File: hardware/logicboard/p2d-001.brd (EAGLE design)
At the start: 100 x 75 mm, 68 parts, among them IC1 74LS06N, IC2 4066N, IC3 MAX3468CPA, J1 MKR, J10 THS, J2 GPIO, J3 Vcc, J4 RLY, J5 SPI, J6 LED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

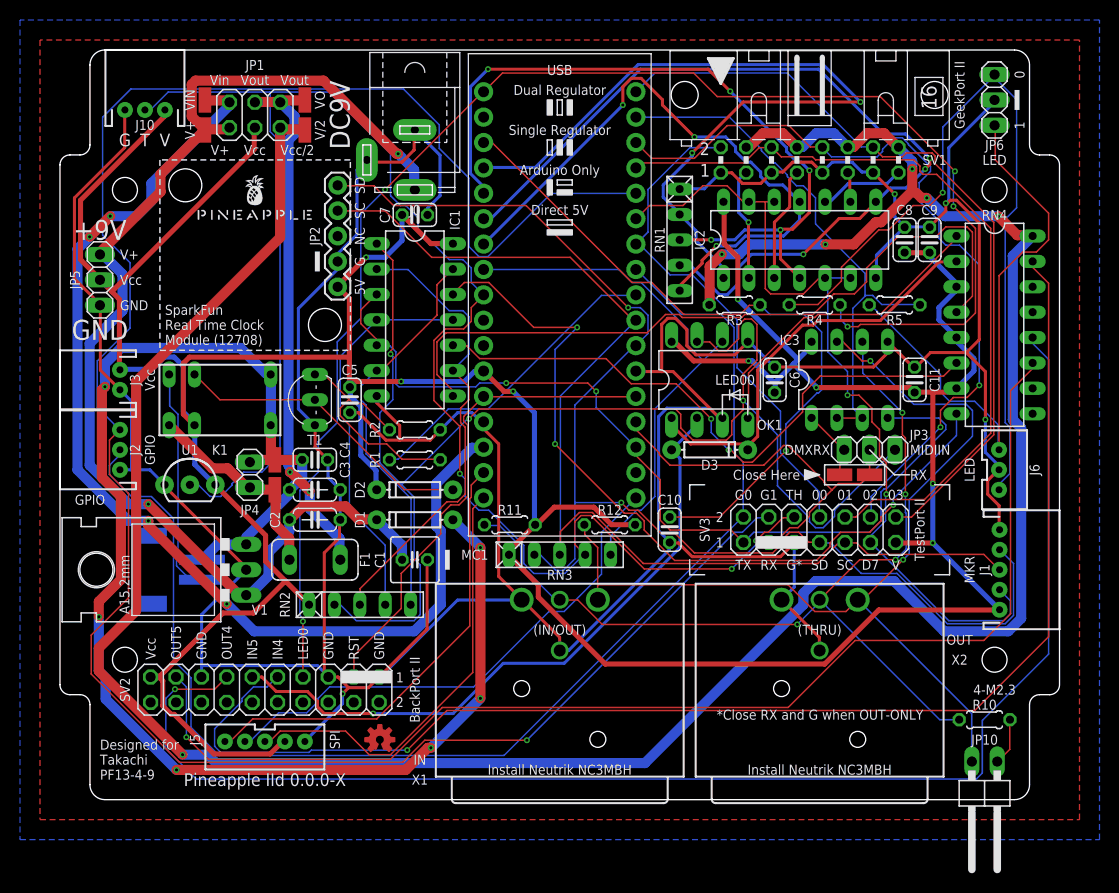
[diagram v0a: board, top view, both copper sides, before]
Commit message: Now DMX's Data- has pull-down R., not pull-up.
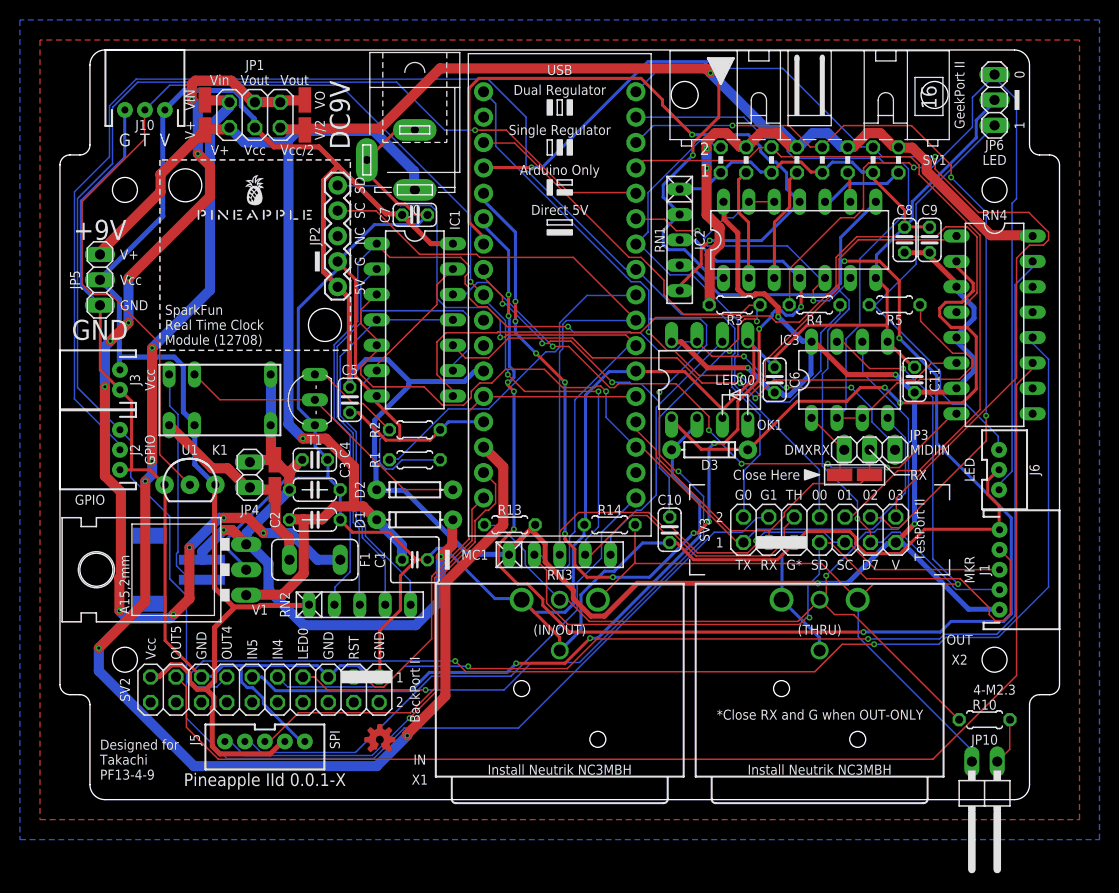
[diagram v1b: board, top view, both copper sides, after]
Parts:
- R13, R14: value 470 -> 22k
- renumbered R11 to R13, R12 to R14
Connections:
- net DATA-: now also R14.2; no longer R14.1
- net GND: now also R14.1
- net VCC: no longer R14.2
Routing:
- net VCC/2: track 275.6 -> 116.1 mm, vias 6 -> 3
- net VOUTRAW: track 146.2 -> 64.9 mm, vias 6 -> 2
- net ANLG2: track 87.7 -> 164.3 mm, vias 3 -> 8
- net VOUT: track 54.0 -> 102.2 mm, vias 2 -> 11
- net VCC: track 395.8 -> 361.9 mm, vias 8 -> 5
- net MIN: track 136.2 -> 103.7 mm, vias 3 -> 4
- net LED1: track 54.9 -> 82.3 mm
- net ANLG1: track 74.2 -> 101.3 mm, vias 5 -> 11
- net VIN: track 110.1 -> 134.6 mm, vias 4 -> 5
- net MISND: track 137.1 -> 113.5 mm, vias 1 -> 2
- net ANLG0: track 78.7 -> 57.2 mm, vias 2 -> 3
- net MOSND: track 142.2 -> 120.9 mm, vias 1 -> 2
- net N$4: track 81.1 -> 62.0 mm, vias 3 -> 5
- net GPIO1: track 213.0 -> 195.1 mm
- net SDA: track 127.5 -> 143.0 mm
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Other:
- board text added: "Pineapple IId 0.0.1-X"
- board text removed: "Pineapple IId 0.0.0-X"

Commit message: Changed DMX pull-up/down resisters to surface mount.
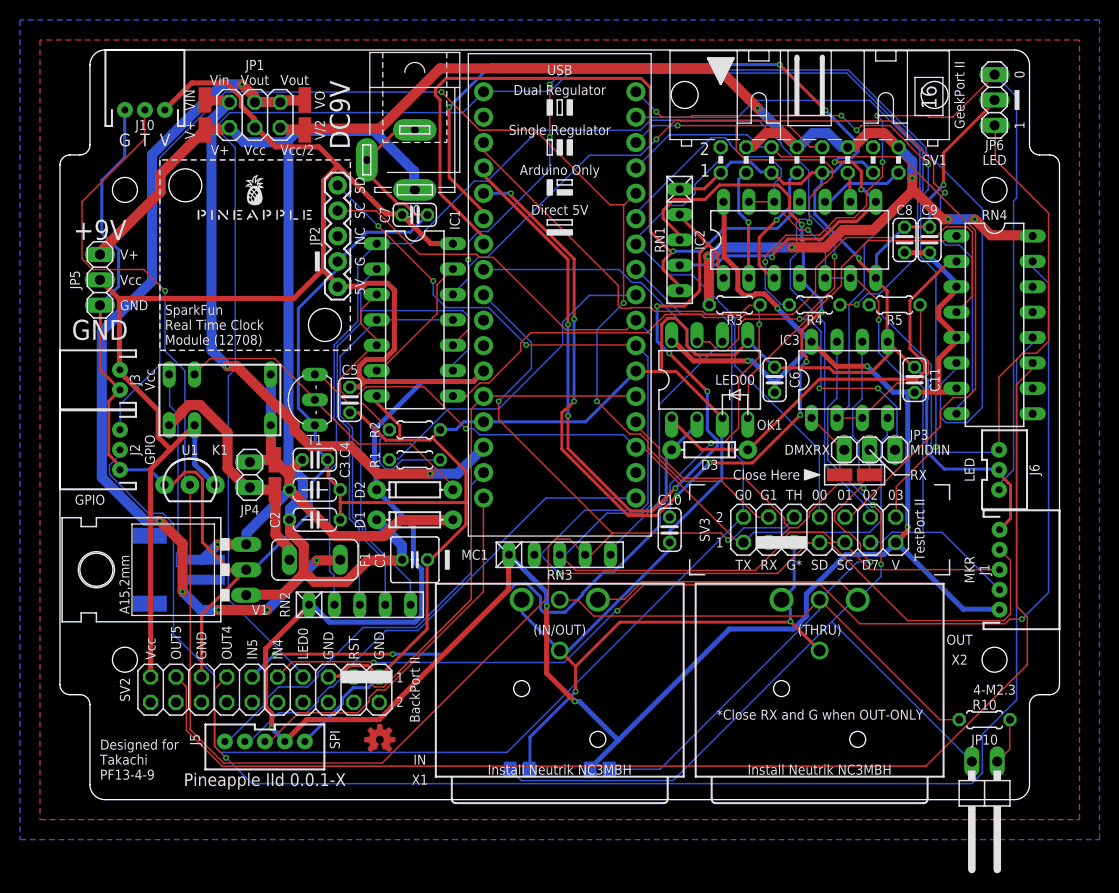
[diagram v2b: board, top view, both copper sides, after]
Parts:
- removed R13, R14: 22k, resistor:0204/5
- added R301, R302: 22k, rcl:M2012
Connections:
- net DATA+: now also R301.1; no longer R13.1
- net DATA-: now also R302.2; no longer R14.2
- net GND: now also R302.1; no longer R14.1
- net VCC: now also R301.2; no longer R13.2
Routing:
- net ANLG2: track 164.3 -> 91.5 mm, vias 8 -> 6
- net VIN: track 134.6 -> 62.0 mm, vias 5 -> 2
- net GPIO1: track 195.1 -> 127.5 mm, vias 1 -> 3
- net VCC: track 361.9 -> 420.5 mm, vias 5 -> 7
- net N$3: track 55.7 -> 111.6 mm, vias 2 -> 3
- net MIN: track 103.7 -> 140.7 mm
- net ANLG0: track 57.2 -> 86.4 mm, vias 3 -> 6
- net THS: track 155.4 -> 180.9 mm
- net N$4: track 62.0 -> 86.5 mm, vias 5 -> 2
- net DATA-: track 96.1 -> 119.4 mm
- net LED1A: track 44.5 -> 61.8 mm
- net LED0: track 138.4 -> 155.8 mm, vias 5 -> 1
- net VOUTRAW: track 64.9 -> 48.2 mm, vias 2 -> 1
- net DATA+: track 91.3 -> 107.5 mm, vias 1 -> 2
- net SDA: track 143.0 -> 127.3 mm, vias 2 -> 4
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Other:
- board text added: "Do not install R301 or R302"

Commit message: Added restricted zone, added J11 for panel-mount XLR con.
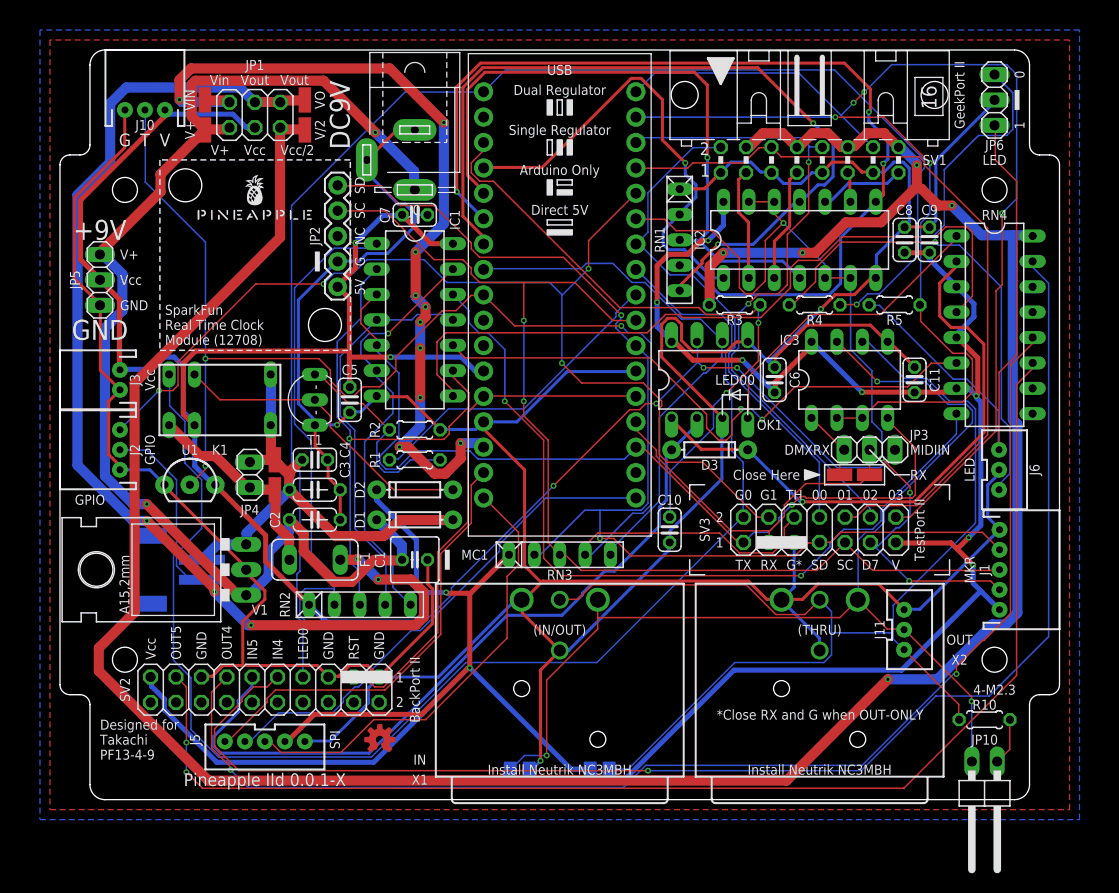
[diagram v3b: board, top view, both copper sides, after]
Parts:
- added J11: LED, SparkFun-Connectors:JST-3-PTH-VERT
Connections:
- net DATA+: now also J11.3
- net DATA-: now also J11.2
- net GND: now also J11.1
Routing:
- net VCC/2: track 123.1 -> 270.8 mm, vias 6 -> 5
- net N$3: track 111.6 -> 60.2 mm, vias 3 -> 2
- net ANLG0: track 86.4 -> 47.1 mm, vias 6 -> 1
- net ANLG1: track 105.0 -> 65.8 mm, vias 9 -> 1
- net THS: track 180.9 -> 144.8 mm
- net DTCT3: track 73.1 -> 97.8 mm, vias 5 -> 3
- net VOUT: track 87.9 -> 112.5 mm, vias 6 -> 5
- net VIN: track 62.0 -> 85.7 mm, vias 2 -> 10
- net GPIO1: track 127.5 -> 104.8 mm, vias 3 -> 4
- net MISND: track 117.7 -> 138.6 mm, vias 3 -> 1
- net V+: track 110.2 -> 126.0 mm, vias 0 -> 2
- net LED0: track 155.8 -> 140.2 mm
- net LED0A: track 85.3 -> 69.9 mm, vias 3 -> 1
- net GND: track 469.0 -> 483.8 mm, vias 4 -> 3
- net N$2: track 44.0 -> 58.3 mm, vias 0 -> 1
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
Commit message: Renamed J11 to XLR.
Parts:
- J11: value LED -> XLR
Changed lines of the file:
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@@
 <attribute name="VALUE" x="47.27" y="0.46" size="1.27" layer="28" rot="MR0"/>
 </element>
-<element name="J11" library="SparkFun-Connectors" library_urn="urn:adsk.eagle:library:513" package="JST-3-PTH-VERT" package3d_urn="urn:adsk.eagle:package:38080/1" value="LED" x="85" y="17" smashed="yes" rot="R270">
+<element name="J11" library="SparkFun-Connectors" library_urn="urn:adsk.eagle:library:513" package="JST-3-PTH-VERT" package3d_urn="urn:adsk.eagle:package:38080/1" value="XLR" x="85" y="17" smashed="yes" rot="R270">
 <attribute name="NAME" x="82" y="17" size="1" layer="25" ratio="20" rot="R270" align="center"/>
 <attribute name="PROD_ID" value="CONN-13230" x="85" y="17" size="1.778" layer="27" rot="R270" display="off"/>
